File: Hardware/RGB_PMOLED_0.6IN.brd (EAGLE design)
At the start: 160 x 100 mm, 22 parts, among them Q1 310mA/60V/1.6Ω, U1 UG-6464TDDBG01, U2 AP3012, U3 3.3V, U4 TXB0104

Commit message: Intemediate commit
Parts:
- removed C10, C11: 0.1uF, SparkFun-Capacitors:0603
- removed C9: 2.2uF, SparkFun-Capacitors:0603
- added C3: 1.0uF, SparkFun-Capacitors:0603
- added C4: 2.2uF, SparkFun-Capacitors:0603
- added C5, C6: 0.1uF, SparkFun-Capacitors:0603
- added C7: 2.2uF/25V, SparkFun-Capacitors:0805
- added R5: 390k, SparkFun-Resistors:0603
- C2: value 1.0uF/25V -> 1.0uF; device SparkFun-Capacitors:0805 -> SparkFun-Capacitors:0603
- U1: value UG-6464TDDBG01 -> UG-6464TDDBG01-EXT; device RGB_OLED:UG-6464TDDBG01 -> RGB_OLED:UG-6464TDDBG01-EXTENDED
- moved J1 254.7 mm to (141.0, 52.1)
- moved U3 226.2 mm to (138.4, 21.6)
- moved R4 222.7 mm to (118.1, 14.0), turned to 90 degrees
- moved R3 220.4 mm to (118.1, 7.62), turned to 180 degrees
- moved Q1 219.7 mm to (118.1, 10.2)
- moved FD2 201.5 mm to (74.9, 74.9)
- moved FD1 201.5 mm to (74.9, 77.5)
- moved LOGO1 201.5 mm to (80.0, 81.3)
- moved U4 191.5 mm to (96.5, 14.0)
- moved C1 164.9 mm to (125.7, 85.1)
- moved L1 164.9 mm to (146.1, 86.4)
- moved U2 164.9 mm to (142.2, 85.1)
- moved C2 164.9 mm to (137.2, 85.1)
- moved D1 164.9 mm to (130.8, 85.1)
- moved R1 164.9 mm to (121.9, 85.1)
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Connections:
- removed net N$12: U1.19
- removed net N$8: U1.2
- removed net N$9: U1.3
- new net N$5: C7.2, U1.3
- net 12V: now also U1.2
- net 3.3V: now also C4.1, C5.1; no longer C10.1, C9.1
- net GND: now also C3.2, C4.2, C5.2, C6.2, C7.1, R5.1, U1.1, U1.19, U1.20; no longer C10.2, C11.2, C9.2
- net N$10: now also C8.1
- net N$11: now also R5.2
- net VIN: now also C3.1, C6.1; no longer C11.1, C8.1

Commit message: First revision
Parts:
- added H1, H2: STAND-OFF, SparkFun-Hardware:STAND-OFF
- added LOGO2, LOGO4: OSHW-LOGOS, SparkFun-Aesthetics:OSHW-LOGO-S
- added LOGO3: SPARKX-LOGO5, 1.81_Greyscale_OLED_Breakout:SPARKX-LARGE
- added U$1, U$2: (no value), buzzard_labels:VIN0
- added U$10, U$11: (no value), buzzard_labels:#RES2
- added U$12, U$13: (no value), buzzard_labels:#CS6
- added U$14, U$9: (no value), buzzard_labels:D##C5
- added U$16: (no value), buzzard_labels:RGB_OLED_64X64_0#6#7
- added U$3, U$4: (no value), buzzard_labels:SDIN3
- added U$5, U$6: (no value), buzzard_labels:SCLK4
- added U$7, U$8: (no value), buzzard_labels:GND1
- C7: value 2.2uF/25V -> 2.2uF
- U1: value UG-6464TDDBG01-EXT -> UG-6464TDDBG01-FLD; device RGB_OLED:UG-6464TDDBG01-EXTENDED -> RGB_OLED:UG-6464TDDBG01-FOLDED
- moved L1 144.9 mm to (19.1, 16.5), flipped to the bottom, turned to 90 degrees
- moved U2 139.2 mm to (19.1, 20.3), flipped to the bottom, turned to 90 degrees
- moved C2 132.2 mm to (19.1, 25.7), flipped to the bottom
- moved D1 131.3 mm to (15.2, 22.9), flipped to the bottom, turned to 270 degrees
- moved J1 130.9 mm to (20.3, 1.27), flipped to the bottom
- moved C3 127.0 mm to (11.4, 20.3), flipped to the bottom
- moved FRAME1 126.7 mm to (34.3, -14.0), flipped to the bottom
- moved C4 125.8 mm to (12.7, 27.9), flipped to the bottom
- moved U3 125.8 mm to (12.7, 24.1), flipped to the bottom
- moved C1 121.4 mm to (19.1, 27.1), flipped to the bottom
- moved R1 120.2 mm to (19.1, 22.9), flipped to the bottom
- moved R2 116.2 mm to (19.1, 24.3), flipped to the bottom, turned to 180 degrees
- moved FD2 103.3 mm to (2.54, 1.27), flipped to the bottom
- moved LOGO1 100.3 mm to (2.54, 17.5), flipped to the bottom, turned to 90 degrees
- moved R4 98.0 mm to (20.3, 7.62), flipped to the bottom, turned to 180 degrees
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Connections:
- removed net !CS!: U4.5
- net !CS: now also U4.2
- net !CS!_HIGH: now also J1.7, U4.13; no longer J1.4, U4.10
- net D/!C!_HIGH: now also J1.6; no longer J1.5
- net GND: now also C7.2; no longer C7.1
- net N$5: now also C7.1; no longer C7.2
- net SCLK_HIGH: now also J1.5; no longer J1.6
- net SDIN: now also U4.5; no longer U4.2
- net SDIN_HIGH: now also J1.4, U4.10; no longer J1.7, U4.13
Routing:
- net GND: track 0.00 -> 93.0 mm, vias 0 -> 9
- net VIN: track 0.00 -> 86.0 mm, vias 0 -> 2
- net 3.3V: track 0.00 -> 46.5 mm, vias 0 -> 2
- net !RES: track 0.00 -> 38.0 mm, vias 0 -> 1
- net 12V: track 0.00 -> 22.4 mm, vias 0 -> 3
- net N$5: track 0.00 -> 14.9 mm, vias 0 -> 1
- net N$11: track 0.00 -> 13.4 mm, vias 0 -> 1
- net !RES!_HIGH: track 0.00 -> 11.8 mm
- net N$2: track 0.00 -> 9.20 mm
- net N$10: track 0.00 -> 8.44 mm, vias 0 -> 1
- net D/!C: track 0.00 -> 7.83 mm, vias 0 -> 1
- net SCLK: track 0.00 -> 7.74 mm, vias 0 -> 1
- net !CS!_HIGH: track 0.00 -> 7.14 mm
- net SDIN: track 0.00 -> 7.01 mm, vias 0 -> 1
- net !CS: track 0.00 -> 6.68 mm, vias 0 -> 1
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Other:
- board size 160 x 100 mm -> 22.9 x 29.2 mm
- board text added: "Owen Lyke"

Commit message: Panelized and gerberified
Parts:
- removed LOGO3: SPARKX-LOGO5, 1.81_Greyscale_OLED_Breakout:SPARKX-LARGE
- removed LOGO4: OSHW-LOGOS, SparkFun-Aesthetics:OSHW-LOGO-S
- added FD3, FD4: FIDUCIAL1X2, SparkFun-Aesthetics:FIDUCIAL-1X2
- added R6: 10k, SparkFun-Resistors:0603
- L1: device 1.81_Greyscale_OLED_Breakout:INDUCTOR_3X3 -> SparkFun-Coils:INDUCTOR_3X3
- U$10, U$11: device buzzard_labels:#RES2 -> buzzard_labels:#RST0
- U$3, U$4: device buzzard_labels:SDIN3 -> buzzard_labels:MOSI1
- U$5, U$6: device buzzard_labels:SCLK4 -> buzzard_labels:SCLK2
- U2: device 1.81_Greyscale_OLED_Breakout:SOT23-5 -> SparkFun-IC-Power:SOT23-5
- moved FRAME1 45.7 mm to (-11.4, -14.0), flipped to the top
- moved FD1 20.3 mm to (1.27, 27.9), flipped to the top
- moved U$16 20.2 mm to (21.5, 7.11), flipped to the bottom
- moved FD2 19.1 mm to (21.6, 1.27), flipped to the top
- moved H2 17.8 mm to (20.3, 26.7), flipped to the top
- moved H1 17.8 mm to (20.3, 5.08), flipped to the top
- moved J1 17.8 mm to (2.54, 1.27), flipped to the top
- moved LOGO1 17.8 mm to (20.3, 17.5), flipped to the top
- moved LOGO2 17.8 mm to (20.3, 9.65), flipped to the top
- moved Q1 17.8 mm to (2.54, 10.2), flipped to the top
- moved R3 17.8 mm to (2.54, 12.7), flipped to the top
- moved R4 17.8 mm to (2.54, 7.62), flipped to the top
- moved U$7 17.8 mm to (2.54, 1.52), flipped to the top
- moved U$8 17.8 mm to (2.54, 1.52), flipped to the bottom
- moved U2 16.5 mm to (2.54, 20.3), flipped to the top
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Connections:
- removed net N$10: C8.1, U1.18
- net !CS: now also R6.1
- net 3.3V: now also C8.1, R6.2, U1.18
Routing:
- net 3.3V: track 46.5 -> 67.8 mm, vias 2 -> 4
- net N$11: track 13.4 -> 25.6 mm, vias 1 -> 2
- net GND: track 93.0 -> 83.7 mm, vias 9 -> 12
- net N$10: track 8.44 -> 0.00 mm, vias 1 -> 0
- net !CS: track 6.68 -> 10.6 mm
- net N$5: track 14.9 -> 17.7 mm
- net VIN: track 86.0 -> 83.4 mm
- net !RES: track 38.0 -> 39.3 mm
- net N$2: track 9.20 -> 10.5 mm
- net 12V: track 22.4 -> 23.5 mm
- net N$3: track 4.53 -> 3.61 mm
- added copper zone on layer 1, net GND
- added copper zone on layer 16, net GND
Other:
- outline, holes or cut-outs redrawn
- board text added: "X01"

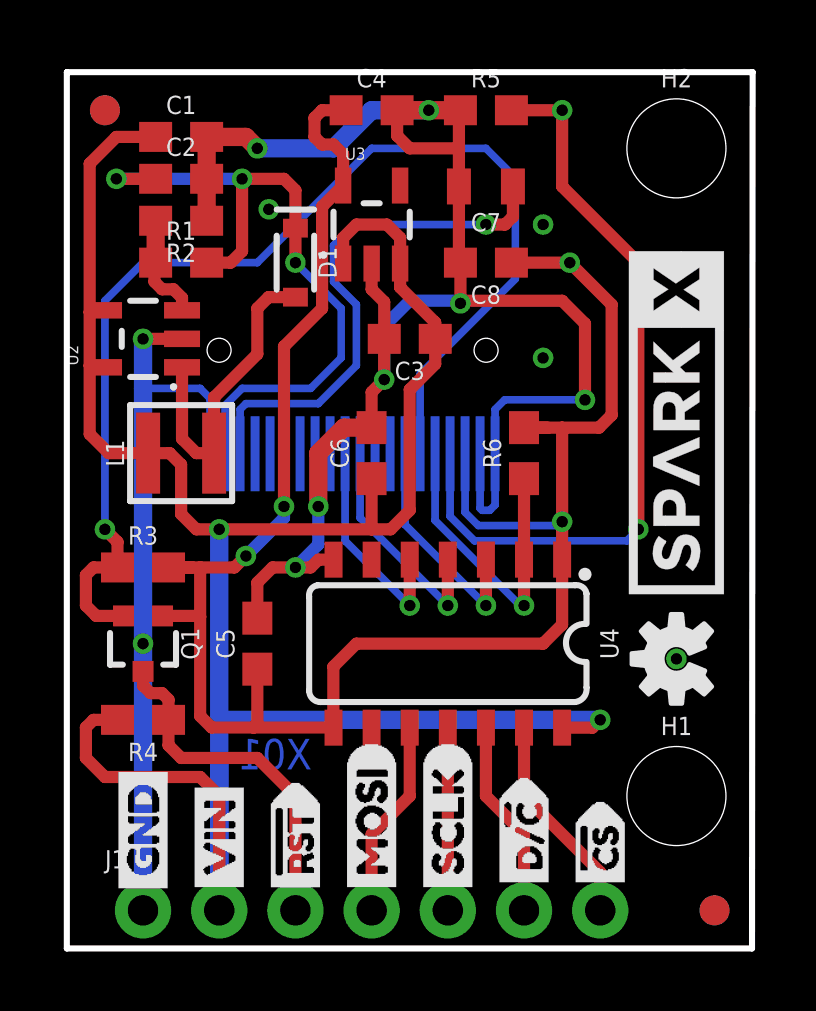
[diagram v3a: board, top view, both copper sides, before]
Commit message: Revision 2 of board using a connector
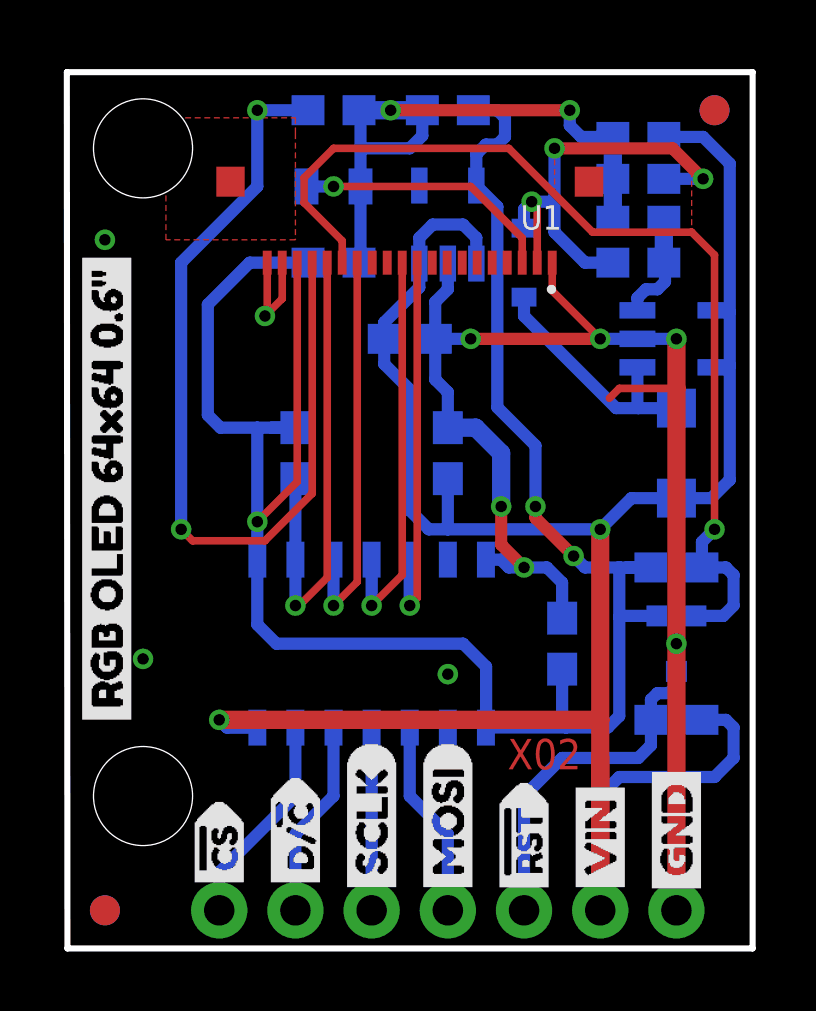
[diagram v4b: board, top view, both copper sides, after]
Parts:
- L1: device SparkFun-Coils:INDUCTOR_3X3 -> SparkFun-Coils:INDUCTOR_4.7UH
- U1: value UG-6464TDDBG01-FLD -> UG-6464TDDBG01; device RGB_OLED:UG-6464TDDBG01-FOLDED -> RGB_OLED:AMPHENOL_10051922-2010ELF
- moved FRAME1 45.7 mm to (34.3, -14.0), flipped to the bottom
- moved FD1 20.3 mm to (21.6, 27.9), flipped to the bottom
- moved FD2 20.3 mm to (1.27, 1.27), flipped to the bottom
- moved FD3 20.3 mm to (1.27, 1.27), flipped to the top
- moved FD4 20.3 mm to (21.6, 27.9), flipped to the top
- moved U$16 20.2 mm to (1.33, 7.11), flipped to the top
- moved H1 17.8 mm to (2.54, 5.08), flipped to the bottom
- moved H2 17.8 mm to (2.54, 26.7), flipped to the bottom
- moved J1 17.8 mm to (20.3, 1.27), flipped to the bottom
- moved LOGO1 17.8 mm to (2.54, 17.5), flipped to the bottom
- moved LOGO2 17.8 mm to (2.54, 9.65), flipped to the bottom
- moved Q1 17.8 mm to (20.3, 10.2), flipped to the bottom
- moved R3 17.8 mm to (20.3, 12.7), flipped to the bottom
- moved R4 17.8 mm to (20.3, 7.62), flipped to the bottom
- moved U$7 17.8 mm to (20.3, 1.52), flipped to the bottom
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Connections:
- net GND: now also U1.P$21, U1.P$22
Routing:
- net GND: track 83.7 -> 73.7 mm
- net N$5: track 17.7 -> 8.72 mm
- net 12V: track 23.5 -> 15.7 mm
- net !RES: track 39.3 -> 33.1 mm
- net SCLK: track 7.80 -> 13.4 mm
- net SDIN: track 7.48 -> 13.1 mm
- net !CS: track 10.6 -> 16.2 mm
- net D/!C: track 7.71 -> 13.3 mm
- net N$11: track 25.6 -> 29.6 mm
- net 3.3V: track 67.8 -> 71.8 mm, vias 4 -> 3
- net N$2: track 10.5 -> 8.35 mm
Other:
- outline, holes or cut-outs redrawn
- board text added: "X02"
- board text removed: "X01"

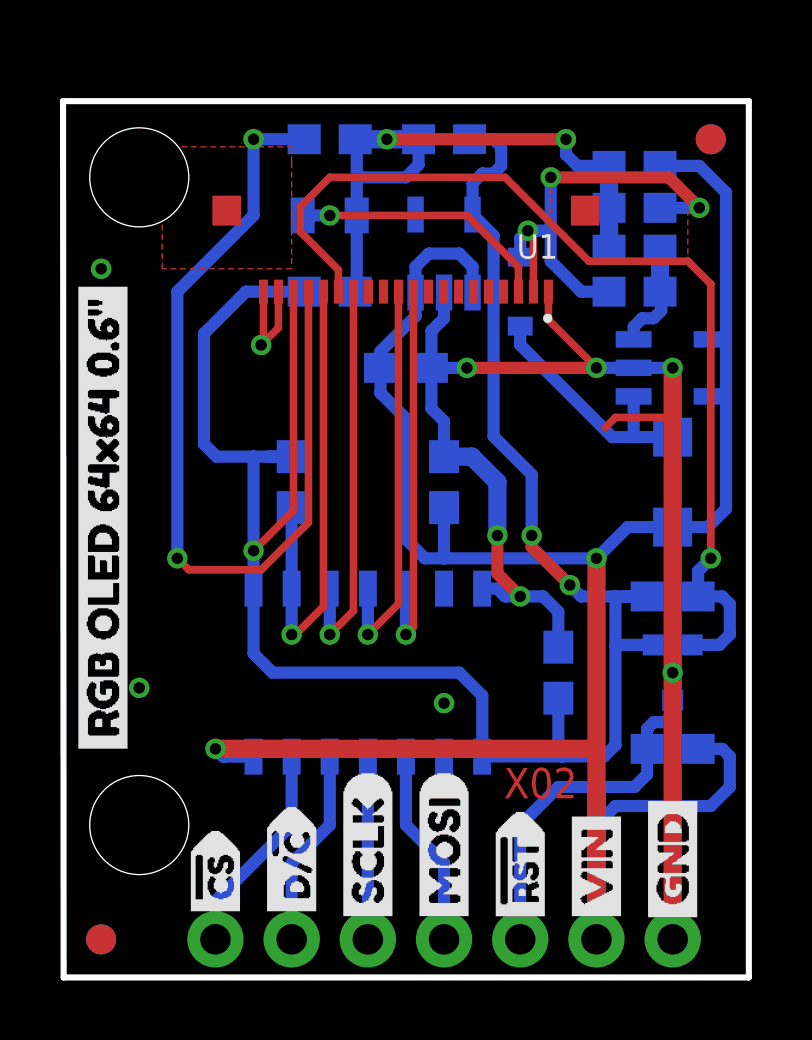
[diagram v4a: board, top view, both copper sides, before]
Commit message: Fixed clearance of 4-40 screw
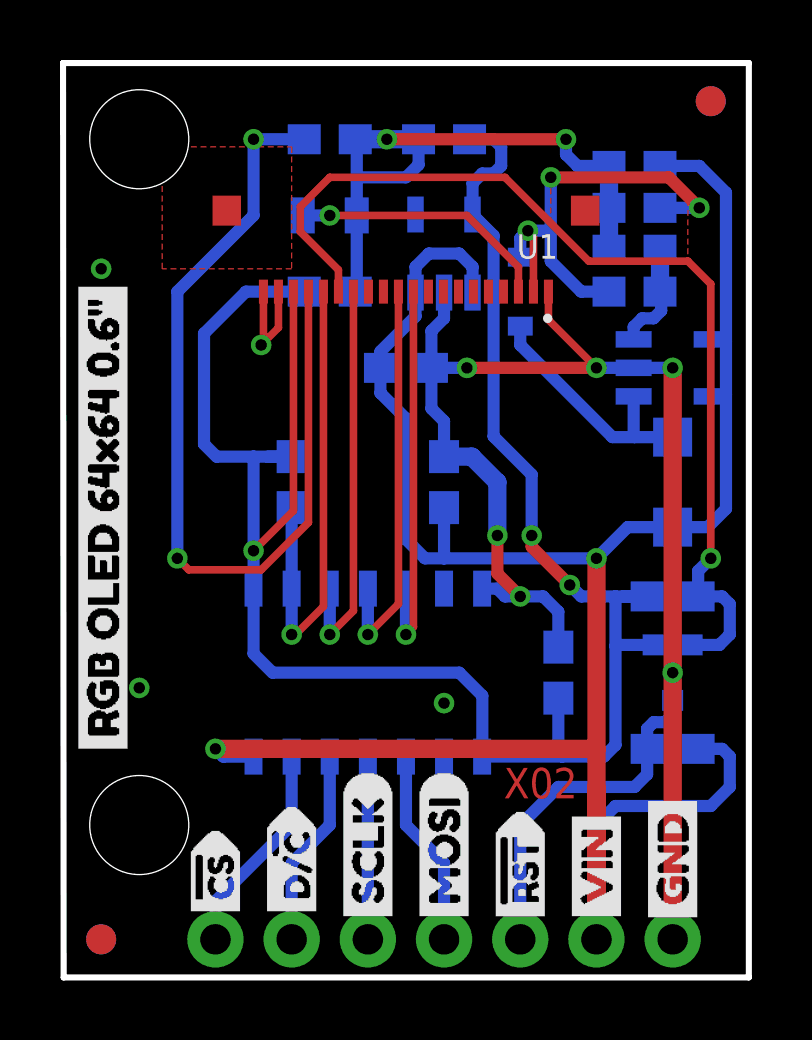
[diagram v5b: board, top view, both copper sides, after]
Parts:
- moved FD1 1.27 mm to (21.6, 29.2)
- moved FD4 1.27 mm to (21.6, 29.2)
- moved H2 1.27 mm to (2.54, 27.9)
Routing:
- net GND: track 73.7 -> 71.3 mm
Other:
- board size 22.9 x 29.2 mm -> 22.9 x 30.5 mm
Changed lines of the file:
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@@
 <setting verticaltext="up"/>
 </settings>
-<grid distance="10" unitdist="mil" unit="mil" style="lines" multiple="1" display="yes" altdistance="0.005" altunitdist="inch" altunit="inch"/>
+<grid distance="0.05" unitdist="inch" unit="mil" style="lines" multiple="1" display="yes" altdistance="0.005" altunitdist="inch" altunit="inch"/>
 <layers>
 <layer number="1" name="Top" color="4" fill="1" visible="yes" active="yes"/>
@@
 <plain>
 <wire x1="22.86" y1="0" x2="0.02" y2="0" width="0.2032" layer="20"/>
-<wire x1="0.02" y1="0" x2="0" y2="29.21" width="0.2032" layer="20"/>
-<wire x1="0" y1="29.21" x2="22.86" y2="29.21" width="0.2032" layer="20"/>
-<wire x1="22.86" y1="29.21" x2="22.86" y2="0" width="0.2032" layer="20"/>
+<wire x1="0.02" y1="0" x2="0" y2="30.48" width="0.2032" layer="20"/>
+<wire x1="0" y1="30.48" x2="22.86" y2="30.48" width="0.2032" layer="20"/>
+<wire x1="22.86" y1="30.48" x2="22.86" y2="0" width="0.2032" layer="20"/>
 <text x="6.35" y="-13.97" size="1.778" layer="52" font="vector" ratio="15" rot="MR0">Owen Lyke</text>
 <text x="17.145" y="6.985" size="1.016" layer="1" font="vector" ratio="15" rot="R180">X02</text>
@@
 </element>
 <element name="LOGO1" library="1.81_Greyscale_OLED_Breakout" package="SPARKX-LARGE" value="SPARKX-LOGO5" x="2.54" y="17.526" rot="MR90"/>
-<element name="FD1" library="SparkFun-Aesthetics" package="FIDUCIAL-1X2" value="FIDUCIAL1X2" x="21.59" y="27.94" rot="MR0"/>
+<element name="FD1" library="SparkFun-Aesthetics" package="FIDUCIAL-1X2" value="FIDUCIAL1X2" x="21.59" y="29.21" rot="MR0"/>
 <element name="FD2" library="SparkFun-Aesthetics" package="FIDUCIAL-1X2" value="FIDUCIAL1X2" x="1.27" y="1.27" rot="MR0"/>
 <element name="Q1" library="SparkFun-DiscreteSemi" package="SOT323" value="310mA/60V/1.6Ω" x="20.32" y="10.16" rot="MR180">
@@
 <element name="LOGO2" library="SparkFun-Aesthetics" package="OSHW-LOGO-S" value="OSHW-LOGOS" x="2.54" y="9.652" rot="MR90"/>
 <element name="H1" library="SparkFun-Hardware" package="STAND-OFF" value="STAND-OFF" x="2.54" y="5.08" rot="MR0"/>
-<element name="H2" library="SparkFun-Hardware" package="STAND-OFF" value="STAND-OFF" x="2.54" y="26.67" rot="MR0"/>
+<element name="H2" library="SparkFun-Hardware" package="STAND-OFF" value="STAND-OFF" x="2.54" y="27.94" rot="MR0"/>
 <element name="U$1" library="buzzard_labels" package="VIN0" value="" x="17.78" y="1.524" rot="MR90"/>
 <element name="U$2" library="buzzard_labels" package="VIN0" value="" x="17.78" y="1.524" rot="R90"/>
@@
 </element>
 <element name="FD3" library="SparkFun-Aesthetics" package="FIDUCIAL-1X2" value="FIDUCIAL1X2" x="1.27" y="1.27"/>
-<element name="FD4" library="SparkFun-Aesthetics" package="FIDUCIAL-1X2" value="FIDUCIAL1X2" x="21.59" y="27.94"/>
+<element name="FD4" library="SparkFun-Aesthetics" package="FIDUCIAL-1X2" value="FIDUCIAL1X2" x="21.59" y="29.21"/>
 <element name="U$10" library="buzzard_labels" package="#RST0" value="" x="15.24" y="1.397" rot="MR90"/>
 <element name="U$11" library="buzzard_labels" package="#RST0" value="" x="15.24" y="1.397" rot="R90"/>
@@
 <wire x1="20.32" y1="1.27" x2="20.32" y2="10.16" width="0.6096" layer="1"/>
 <via x="20.32" y="20.32" extent="1-16" drill="0.381"/>
-<wire x1="20.32" y1="10.16" x2="20.32" y2="18.669" width="0.6096" layer="1"/>
-<wire x1="20.32" y1="18.669" x2="20.32" y2="20.32" width="0.6096" layer="1"/>
+<wire x1="20.32" y1="10.16" x2="20.32" y2="20.32" width="0.6096" layer="1"/>
 <via x="15.24" y="12.7" extent="1-16" drill="0.381"/>
 <wire x1="13.628" y1="17.36" x2="12.7" y2="17.36" width="0.6096" layer="16"/>
@@
 <polygon width="0.2032" layer="16" isolate="0.3048">
 <vertex x="0" y="0"/>
-<vertex x="0" y="29.21"/>
-<vertex x="22.86" y="29.21"/>
+<vertex x="0" y="30.48"/>
+<vertex x="22.86" y="30.48"/>
 <vertex x="22.86" y="0"/>
 </polygon>
 <polygon width="0.2032" layer="1" isolate="0.3048">
 <vertex x="0" y="0"/>
-<vertex x="0" y="29.21"/>
-<vertex x="22.86" y="29.21"/>
+<vertex x="0" y="30.48"/>
+<vertex x="22.86" y="30.48"/>
 <vertex x="22.86" y="0"/>
 </polygon>
-<wire x1="18.085" y1="18.339" x2="18.415" y2="18.669" width="0.254" layer="1"/>
-<wire x1="18.415" y1="18.669" x2="20.32" y2="18.669" width="0.254" layer="1"/>
 <wire x1="15.24" y1="12.7" x2="14.478" y2="13.462" width="0.4064" layer="1"/>
 <wire x1="14.478" y1="13.462" x2="14.478" y2="14.732" width="0.4064" layer="1"/>
@@
 </polygon>
 <polygon width="0.1016" layer="1" isolate="0.3048" thermals="no">
-<vertex x="7.62" y="27.178"/>
+<vertex x="7.62" y="27.686"/>
 <vertex x="7.62" y="23.622"/>
 <vertex x="3.302" y="23.622"/>
-<vertex x="3.302" y="27.178"/>
 <vertex x="3.302" y="27.686"/>
-<vertex x="7.62" y="27.686"/>
 </polygon>
 <via x="1.27" y="23.622" extent="1-16" drill="0.381"/>
@@
 </signal>
 </signals>
-<errors>
-</errors>
 </board>
 </drawing>

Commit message: Cleaned up documentation
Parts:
- moved FRAME1 45.7 mm to (-11.4, -14.0), flipped to the top
- moved FD1 20.3 mm to (1.27, 29.2), flipped to the top
- moved FD2 20.3 mm to (21.6, 1.27), flipped to the top
- moved FD3 20.3 mm to (21.6, 1.27), flipped to the bottom
- moved FD4 20.3 mm to (1.27, 29.2), flipped to the bottom
- moved U$16 20.2 mm to (21.5, 7.11), flipped to the bottom
- moved H1 17.8 mm to (20.3, 5.08), flipped to the top
- moved H2 17.8 mm to (20.3, 27.9), flipped to the top
- moved J1 17.8 mm to (2.54, 1.27), flipped to the top
- moved L1 17.8 mm to (2.54, 16.5), flipped to the top
- moved LOGO1 17.8 mm to (20.3, 17.5), flipped to the top
- moved LOGO2 17.8 mm to (20.3, 9.65), flipped to the top
- moved Q1 17.8 mm to (2.54, 10.2), flipped to the top
- moved R3 17.8 mm to (2.54, 12.7), flipped to the top
- moved R4 17.8 mm to (2.54, 7.62), flipped to the top
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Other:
- outline, holes or cut-outs redrawn
